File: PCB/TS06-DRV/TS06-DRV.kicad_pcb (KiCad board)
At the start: 2 copper layers, 191.4 x 100 mm, 103 parts, among them J1 PH 6 vertical, U1 Arduino Nano, U10 TLP627, U11 TC4420, U12 LM393, U13 DS3231 mini, U14 R-78E5.0-1.0, U15 K155ID1, U16 K155ID1, U17 K155ID1, U2 K155ID1, U3 MCP23017-E/SP, U5 TLP627, U6 TLP627, U7 TLP627, U8 TLP627, U9 TLP627

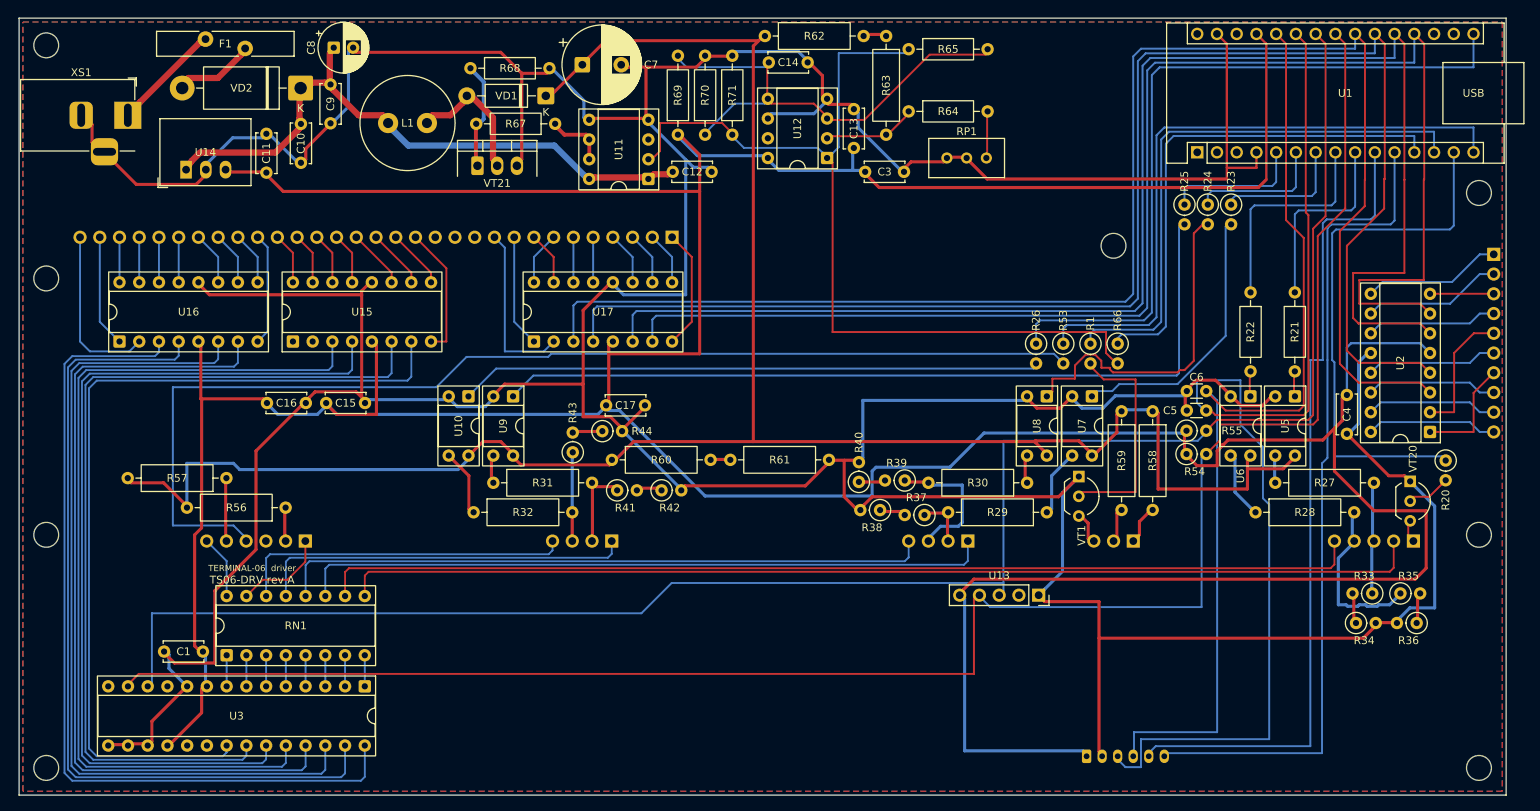
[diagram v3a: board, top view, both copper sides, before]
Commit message: TS06-DRV rev B: routed - round 13, 0 nets sharing, 0 unrouted; board, rules and schematic written
The route of run r3 (PYTHONHASHSEED=0, the RC block of OPTIONS.md option 3),
polished (30 nets shorter), saved in tools/mkpcb_drv_routes.json, and the board
regenerated from it: check() 0 problems, 0 cathode pads under 0.5 mm, check_mate()
clean, 1164 segments, 0 vias. TS06-DRV.kicad_dru carries the 0.8 mm HV pad rule.
Schematic regenerated by tools/mksch_pair.py; BOMs unchanged by tools/bom_pair.py.

State: board written from a converged route; verify_pair not yet run.
Blocker: none.
Next: verify_pair.sh, scorecard, README row.

Co-Authored-By: Claude Opus 5.5 <noreply@anthropic.com>
Claude-Session: https://claude.ai/code/session_01WoV3gyAFgmtuk6W6Dr4bdA
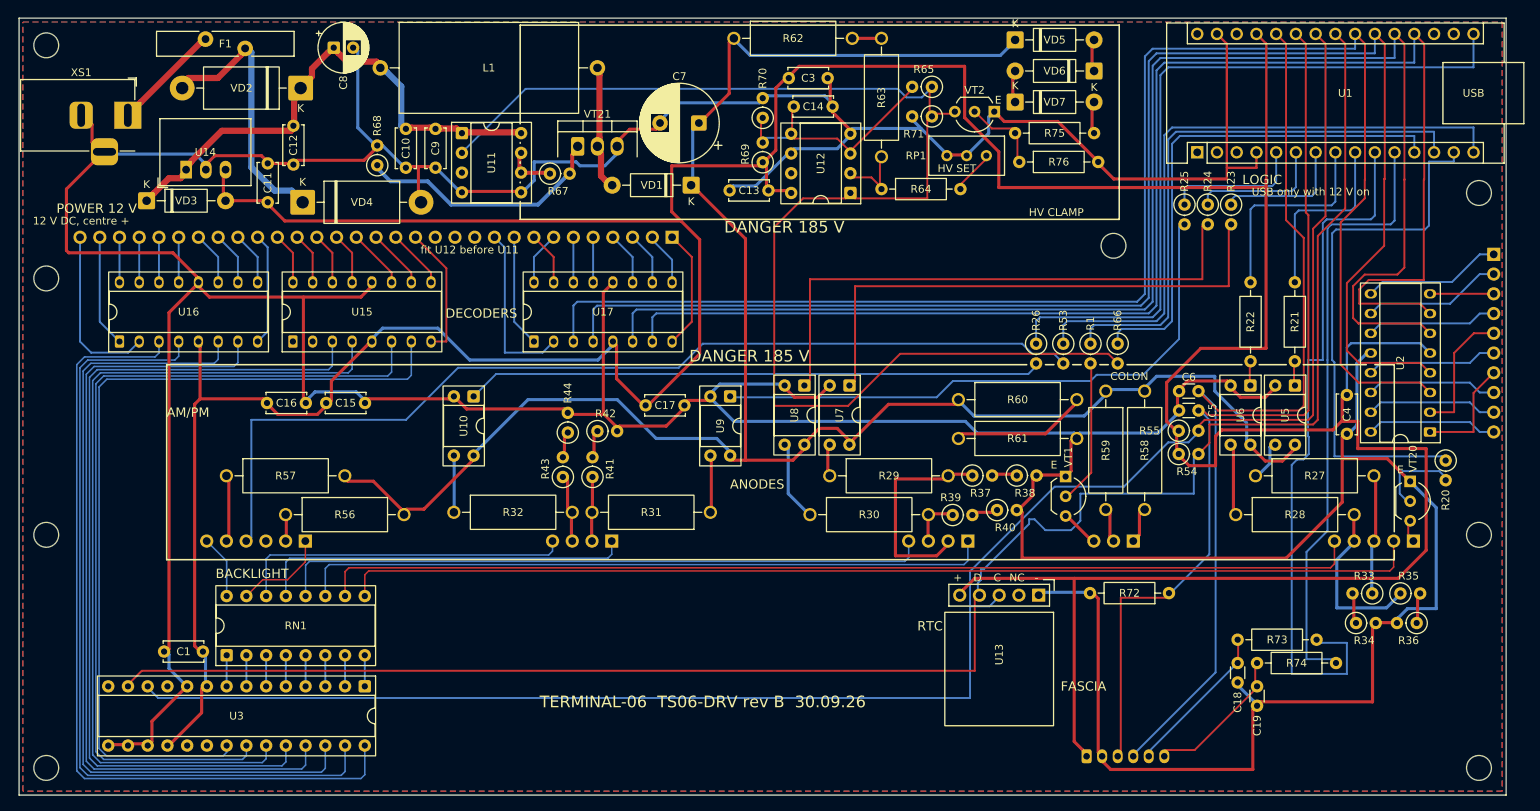
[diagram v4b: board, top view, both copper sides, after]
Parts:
- added C18: 10n, TS06:TS06_C_Disc_P2.50mm_R270, F.Cu at (156.8, 83.0)
- added C19: 10n, TS06:TS06_C_Disc_P2.50mm_R270, F.Cu at (159.3, 86.0)
- added R72: 1M, TS06:TS06_R_Axial_DIN0207_P10.16mm_R180, F.Cu at (148.0, 74.0)
- added R73: 1k, TS06:TS06_R_Axial_DIN0207_P10.16mm_R180, F.Cu at (167.0, 80.0)
- added R74: 1k, TS06:TS06_R_Axial_DIN0207_P10.16mm_R180, F.Cu at (169.5, 83.0)
- added R75: 100k, TS06:TS06_R_Axial_DIN0207_P10.16mm_R180, F.Cu at (138.4, 14.8)
- added R76: 10k, TS06:TS06_R_Axial_DIN0207_P10.16mm, F.Cu at (128.7, 18.5)
- added VD3: 1N5819, TS06:TS06_D_DO-41_P10.16mm, F.Cu at (16.4, 23.5)
- added VD4: 1.5KE18A, TS06:TS06_D_DO-201AD_P15.24mm, F.Cu at (36.5, 23.7)
- added VD5: 1N4762A, TS06:TS06_D_DO-41_P10.16mm, F.Cu at (128.2, 2.80)
- added VD6: 1N4762A, TS06:TS06_D_DO-41_P10.16mm_R180, F.Cu at (138.4, 6.80)
- added VD7: 1N4761A, TS06:TS06_D_DO-41_P10.16mm, F.Cu at (128.2, 10.8)
- added VT2: 2N3904, TS06:TS06_TO-92_Inline_Wide_R180, F.Cu at (125.5, 12.0)
- C12: footprint TS06:TS06_C_Disc_P5.00mm -> TS06:TS06_C_Disc_P5.00mm_R270
- C13: footprint TS06:TS06_C_Disc_P5.00mm_R90 -> TS06:TS06_C_Disc_P5.00mm_R180
- C7: footprint TS06:TS06_CP_Radial_D10.0mm_P5.00mm -> TS06:TS06_CP_Radial_D10.0mm_P5.00mm_R180
- L1: value 220u 2A -> 220u 1.8A 5900-221-RC; footprint TS06:TS06_L_Radial_D12.0mm_P5.00mm -> TS06:TS06_L_Axial_D11.5mm_L22.9mm_P27.94mm
- R27, R28, R32, R60, R61, R62: footprint TS06:TS06_R_Axial_DIN0309_P12.70mm -> TS06:TS06_R_Axial_MLT-0.5_P15.24mm
- R29, R30, R56, R57: footprint TS06:TS06_R_Axial_DIN0309_P12.70mm_R180 -> TS06:TS06_R_Axial_MLT-0.5_P15.24mm
- R31: footprint TS06:TS06_R_Axial_DIN0309_P12.70mm -> TS06:TS06_R_Axial_MLT-0.5_P15.24mm_R180
- R37, R38, R39: footprint TS06:TS06_R_Axial_DIN0207_P2.54mm_Vertical_R180 -> TS06:TS06_R_Axial_DIN0207_P2.54mm_Vertical
- R40: footprint TS06:TS06_R_Axial_DIN0207_P2.54mm_Vertical_R90 -> TS06:TS06_R_Axial_DIN0207_P2.54mm_Vertical
- R41, R44: footprint TS06:TS06_R_Axial_DIN0207_P2.54mm_Vertical -> TS06:TS06_R_Axial_DIN0207_P2.54mm_Vertical_R90
- R58, R59, R63: footprint TS06:TS06_R_Axial_DIN0309_P12.70mm_R270 -> TS06:TS06_R_Axial_MLT-0.5_P15.24mm_R270
- R65: footprint TS06:TS06_R_Axial_DIN0207_P10.16mm -> TS06:TS06_R_Axial_DIN0207_P2.54mm_Vertical_R180
- R67: footprint TS06:TS06_R_Axial_DIN0207_P10.16mm_R180 -> TS06:TS06_R_Axial_DIN0207_P2.54mm_Vertical
- R68: footprint TS06:TS06_R_Axial_DIN0207_P10.16mm -> TS06:TS06_R_Axial_DIN0207_P2.54mm_Vertical_R90
- R69, R70: footprint TS06:TS06_R_Axial_DIN0207_P10.16mm_R90 -> TS06:TS06_R_Axial_DIN0207_P2.54mm_Vertical_R90
- R71: footprint TS06:TS06_R_Axial_DIN0207_P10.16mm_R90 -> TS06:TS06_R_Axial_DIN0207_P2.54mm_Vertical_R180
- U11: footprint TS06:TS06_DIP-8_W7.62mm_Socket_R180 -> TS06:TS06_DIP-8_W7.62mm_Socket
- U13: footprint TS06:TS06_PinSocket_1x05_R270 -> TS06:TS06_PinHeader_1x05_DS3231_R270
- U15, U16, U17: footprint TS06:TS06_DIP-16_W7.62mm_Socket_R90 -> TS06:TS06_DIP-16_W7.62mm_Socket_Oval_R90
- U2: footprint TS06:TS06_DIP-16_W7.62mm_Socket_R180 -> TS06:TS06_DIP-16_W7.62mm_Socket_Oval_R180
- moved C12 49.2 mm to (35.3, 13.8)
- moved R60 45.3 mm to (120.9, 49.1)
- moved U7 31.2 mm to (106.9, 47.3)
- moved U8 31.2 mm to (101.1, 47.3)
- moved R61 29.5 mm to (120.9, 54.1)
- moved R29 28.3 mm to (104.3, 58.9)
- moved R30 28.2 mm to (101.8, 63.9)
- moved R31 28.2 mm to (89.0, 63.6)
- moved U9 27.9 mm to (91.5, 48.7)
- moved R71 25.8 mm to (117.5, 12.7)
- moved U11 24.7 mm to (57.0, 14.8)
- moved VD1 22.0 mm to (86.5, 21.5)
- moved R38 18.1 mm to (128.4, 58.9)
- moved R40 18.1 mm to (125.9, 63.3)
- moved R68 17.3 mm to (46.1, 18.9)
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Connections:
- J1 pad 5: D7 -> D7_J
- J1 pad 6: D8 -> D8_J
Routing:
- net PWM_G: track 115.0 -> 175.2 mm
- net GND: track 726.7 -> 771.8 mm
- net +5V: track 598.8 -> 560.7 mm
- net OPT_M10: track 35.3 -> 69.2 mm
- net OPT_S10: track 106.6 -> 76.1 mm
- net VREF: track 61.1 -> 31.6 mm
- net OPT_M1: track 44.0 -> 72.1 mm
- net D8: track 106.1 -> 78.4 mm
- net A6: track 144.4 -> 117.2 mm
- net VIN_F: track 10.5 -> 34.8 mm
- net ANODE_M10: track 6.81 -> 27.7 mm
- net D7_J: track 0.00 -> 19.7 mm
- net M_A: track 145.1 -> 125.6 mm
- net D8_J: track 0.00 -> 19.1 mm
- net GATE: track 13.8 -> 32.5 mm
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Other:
- board text added: "+"
- board text added: "-"
- board text added: "1"
- board text added: "1 +5V 2 GND 3 A6 4 A7 5 D7 6 D8"
- board text added: "12 V DC, centre +"
- board text added: "AM/PM"
- board text added: "ANODES"
- board text added: "BACKLIGHT"
- board text added: "C"
- board text added: "COLON"
- board text added: "D"
- board text added: "DANGER 185 V"
- board text added: "DECODERS"
- board text added: "E"
- board text added: "FASCIA"
- board text added: "HV CLAMP"
- board text added: "HV SET"
- board text added: "LOGIC"
- board text added: "NC"
- board text added: "POWER 12 V"
- board text added: "RTC"
- board text added: "TERMINAL-06 TS06-DRV rev B 30.09.26"
- board text added: "USB only with 12 V on"
- board text added: "fit U12 before U11"
- board text removed: "TERMINAL-06 driver"
- board text removed: "TS06-DRV rev A"
